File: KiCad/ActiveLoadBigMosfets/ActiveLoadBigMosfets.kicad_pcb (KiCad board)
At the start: 2 copper layers, 145 x 70 mm, 170 parts, among them J1 TouchPanel, J2 PowerInput, J3 SWD, J4 RVT28AETNWC00, J5 JTAG, J6 FanOut, J7 PowerInput2, J8 PowerInput3, J9 PowerInput4, Q1 IRLML2502, Q10 IXFK44N50P, Q11 IXFK44N50P, Q12 IXFK44N50P, Q13 IXFK44N50P, Q14 IXFK44N50P, Q2 IRLML2244, Q3 IRLML2244, Q4 IRLML2502, Q5 IRLML2502, Q6 IRLML2502, Q7 IRLML2502, Q8 IRLML2502, Q9 IXFK44N50P, SW1 Rotary_Encoder_Switch, SW2 SW_Push, U1 LMR14020, U2 MCP1825S, U3 STM32L151RBTxA, U4 LM2735YMF, U5 TLV2374, U6 TLV2374, U7 TLV2374, U8 TC74, U9 INA233, Y1 Crystal

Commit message: More pcb work
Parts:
- added J10: I2C, Connector_PinHeader_2.54mm:PinHeader_1x04_P2.54mm_Vertical, F.Cu at (82.5, 31.0)
- C38, U9: moved to F.Cu
- FL1, FL2: footprint Filter:Filter_Murata_BNX025 -> JPInductors:Filter_Murata_BNX025
- L3: footprint Inductor_SMD:L_Wuerth_WE-PDF -> JPInductors:L_Wuerth_WE-PDF_Handsoldering
- R1, R43, R45, R46, R49, R50, R55, R63: footprint Resistor_SMD:R_2512_6332Metric -> Resistor_SMD:R_2512_6332Metric_Pad1.52x3.35mm_HandSolder
- U4: footprint Package_TO_SOT_SMD:SOT-23-5 -> Package_TO_SOT_SMD:SOT-23-5_HandSoldering
- moved C19 24.3 mm to (60.6, 60.8)
- moved C20 24.3 mm to (58.7, 60.8)
- moved C22 24.3 mm to (72.0, 60.8)
- moved FL1 24.3 mm to (47.0, 61.6)
- moved U2 24.3 mm to (65.7, 60.8)
- moved C21 24.3 mm to (75.6, 61.0)
- moved L2 20.3 mm to (24.8, 54.0), turned to 0 degrees
- moved R9 19.9 mm to (38.5, 44.6), turned to 90 degrees
- moved R11 18.9 mm to (37.3, 34.7), turned to 0 degrees
- moved R13 18.2 mm to (37.8, 37.8), turned to 270 degrees
- moved R14 18.1 mm to (37.8, 41.4), turned to 90 degrees
- moved C10 17.2 mm to (36.4, 44.6), turned to 90 degrees
- moved C13 17.1 mm to (31.1, 29.8), turned to 180 degrees
- moved C9 15.0 mm to (34.2, 34.9), turned to 180 degrees
- moved C16 14.0 mm to (34.0, 44.5), turned to 180 degrees
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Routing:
- net +4V: track 107.3 -> 47.3 mm
- net GNDD: track 593.5 -> 546.2 mm, vias 23 -> 22
- net Net-(C10-Pad1): track 55.2 -> 11.4 mm
- net GND: track 225.7 -> 188.3 mm
- net PowerIn+: track 11.9 -> 21.5 mm, vias 0 -> 1
- net +3V3: track 280.6 -> 287.5 mm, vias 20 -> 22
- net PowerIn-: track 239.0 -> 232.7 mm, vias 0 -> 1
- net SCL: track 98.0 -> 102.0 mm, vias 6 -> 5
- net Net-(C8-Pad1): track 17.2 -> 13.7 mm
- net SDA: track 100.3 -> 102.7 mm, vias 4 -> 3
- net Net-(C8-Pad2): track 2.31 -> 0.00 mm
- net GNDA: track 192.1 -> 190.1 mm
- net TP_Interrupt: track 25.9 -> 24.3 mm
- net TP_Reset: track 26.9 -> 25.6 mm
- net SWCLK: track 85.3 -> 84.3 mm
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- removed copper zone on B.Cu, net GND
- removed copper zone on F.Cu, net GND

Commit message: More pcb work
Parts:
- J10: moved to B.Cu
- R48, R53, R54, R56, R57, R61: moved to F.Cu
- moved C37 38.5 mm to (84.1, 18.8)
- moved U8 38.5 mm to (89.8, 21.3)
- moved R60 3.70 mm to (106.5, 19.3)
- moved D4 3.70 mm to (106.4, 21.7)
- moved C33 3.36 mm to (70.1, 15.5)
- moved C34 3.19 mm to (71.9, 15.5)
- moved R38 2.82 mm to (23.9, 9.14)
- moved R39 2.82 mm to (26.9, 9.14)
- moved R40 2.82 mm to (69.6, 9.14)
- moved R41 2.82 mm to (72.6, 9.14)
- moved R44 2.82 mm to (119.6, 9.14)
- moved R42 2.82 mm to (116.6, 9.14)
- moved C36 2.59 mm to (118.9, 15.5)
- moved C35 2.55 mm to (117.1, 15.5)
- moved R26 2.54 mm to (20.3, 14.0)
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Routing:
- net PowerIn-: track 232.7 -> 164.7 mm
- net LoadLevel: track 138.2 -> 120.4 mm, vias 9 -> 6
- net GNDA: track 190.1 -> 172.7 mm, vias 7 -> 4
- net GNDD: track 546.2 -> 529.7 mm, vias 22 -> 21
- net +3V3: track 287.5 -> 276.5 mm, vias 22 -> 21
- net LED: track 42.2 -> 31.2 mm
- net SDA: track 102.7 -> 92.6 mm
- net SCL: track 102.0 -> 93.2 mm
- net +12V: track 182.2 -> 176.1 mm
- net GND: track 188.3 -> 193.4 mm
- net Net-(Q10-Pad3): track 9.67 -> 14.0 mm, vias 0 -> 1
- net Net-(Q12-Pad3): track 10.7 -> 14.6 mm, vias 0 -> 1
- net Net-(C39-Pad2): track 8.35 -> 11.5 mm, vias 0 -> 1
- net Net-(Q14-Pad3): track 10.7 -> 13.7 mm, vias 0 -> 1
- net Net-(Q11-Pad3): track 20.8 -> 23.4 mm
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
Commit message: PCB work
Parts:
- added REF**: RVT28AETNWC00-Folded, JPDisplays:RVT28AETNWC00-Folded, F.Cu at (72.9, 69.8)
- J4: footprint JPConnectors:Hirose_FH12-50S-0.5SH_1x50-1MP_P0.50mm_Horizontal -> JPConnectors:Molex-50S-0.5SH_1x50-P0.50mm_Horizontal
- SW2: footprint Button_Switch_SMD:SW_SPST_EVQP0 -> Button_Switch_SMD:SW_SPST_B3S-1000
- U8: footprint Package_TO_SOT_THT:TO-220-5_Vertical -> Connector_PinHeader_2.54mm:PinHeader_1x05_P2.54mm_Vertical
- moved J10 48.7 mm to (34.5, 22.6)
- moved C37 44.4 mm to (39.6, 18.8), turned to 270 degrees
- moved U8 37.7 mm to (52.3, 17.5), turned to 90 degrees
- moved C29 20.7 mm to (121.4, 59.1), turned to 270 degrees
- moved C24 16.2 mm to (72.4, 48.0), turned to 270 degrees
- moved C15 14.9 mm to (75.7, 31.9), turned to 90 degrees
- moved R65 14.5 mm to (77.1, 31.9), turned to 90 degrees
- moved R64 14.3 mm to (78.5, 31.9), turned to 90 degrees
- moved C27 13.8 mm to (116.7, 61.0), turned to 270 degrees
- moved R19 12.8 mm to (70.9, 48.0), turned to 270 degrees
- moved C14 11.5 mm to (115.1, 61.0), turned to 270 degrees
- moved D2 11.3 mm to (113.8, 57.1), turned to 180 degrees
- moved L3 11.1 mm to (104.9, 54.0), turned to 0 degrees
- moved R25 10.9 mm to (114.3, 63.5), turned to 180 degrees
- moved C26 10.4 mm to (112.5, 66.0), turned to 90 degrees
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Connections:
- U3 pad 49: Net-(U3-Pad49) -> /LCD_RESET
- U3 pad 50: /LCD_RESET -> Net-(U3-Pad50)
- U8 pad 2: SCL -> SDA
- U8 pad 4: SDA -> SCL
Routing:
- net +4V: track 47.3 -> 104.4 mm, vias 4 -> 6
- net TP_X_Ctrl: track 3.03 -> 54.7 mm, vias 0 -> 2
- net TP_Y_Ctrl: track 3.42 -> 51.4 mm, vias 0 -> 2
- net TP_SenseX-: track 8.03 -> 55.2 mm, vias 1 -> 2
- net GNDD: track 529.7 -> 574.4 mm, vias 21 -> 25
- net TP_SenseY-: track 12.7 -> 55.9 mm, vias 1 -> 2
- net GND: track 193.4 -> 229.8 mm, vias 1 -> 2
- net Net-(C10-Pad1): track 11.4 -> 44.5 mm
- net InaAlert: track 70.9 -> 50.2 mm, vias 7 -> 3
- net PowerIn-: track 164.7 -> 184.0 mm
- net Net-(R64-Pad2): track 36.9 -> 53.4 mm
- net +12V: track 176.1 -> 160.9 mm, vias 5 -> 7
- net LED: track 31.2 -> 43.7 mm
- net FanPWD: track 35.7 -> 48.1 mm
- net FanSensor: track 35.3 -> 46.8 mm
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- added copper zone on B.Cu, net GND
- added copper zone on F.Cu, net GND
- added copper zone on B.Cu, net GNDD
- added copper zone on F.Cu, net GNDD
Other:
- board size 145 x 70 mm -> 144.8 x 70 mm
- net class DigitalPower added: clearance 0.14, trace_width 0.6096, via_dia 0.6, via_drill 0.4
- board text added: "1"
- board text added: "3V3"
- board text added: "50"
- board text added: "6"
- board text added: "ActveLoadBigMosfet v1 JP, 10.04.2020"
- board text added: "Fan"
- board text added: "Gnd"
- board text added: "JTAG"
- board text added: "NRST"
- board text added: "SCL"
- board text added: "SDA"
- board text added: "STM32L151RBTxA"
- board text added: "SWCLK"
- board text added: "SWD"
- board text added: "SWDIO"
- board text added: "SWDO"
- board text added: "nc"

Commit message: PCB work
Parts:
- removed REF**: RVT28AETNWC00-Folded, JPDisplays:RVT28AETNWC00-Folded
- moved R43 1.40 mm to (13.3, 9.65)
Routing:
- net Net-(Q9-Pad3): track 24.0 -> 27.9 mm
- net GND: track 229.8 -> 229.3 mm
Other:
- board text added: "ActiveLoadBigMosfets v1 JP, 10.04.2020"
- board text removed: "ActveLoadBigMosfet v1 JP, 10.04.2020"

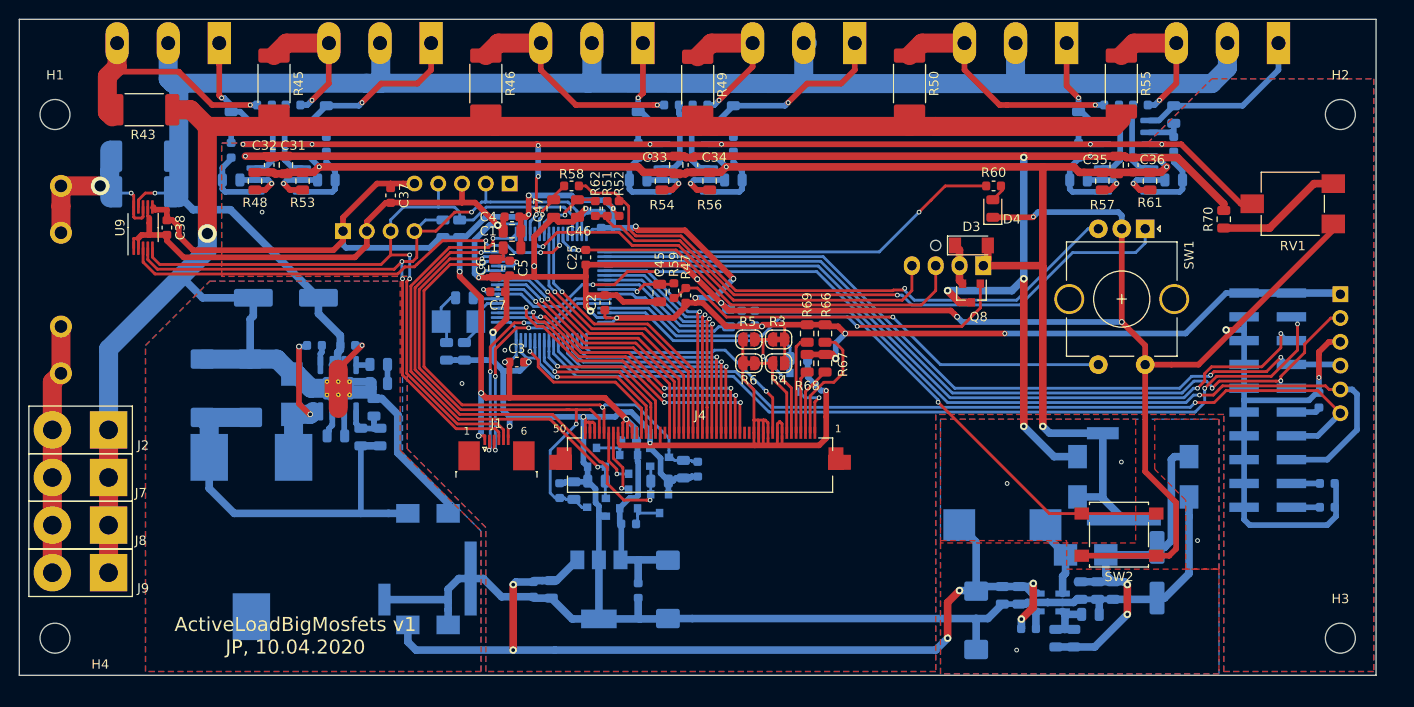
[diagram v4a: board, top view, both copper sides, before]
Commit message: Latest PCB changes. STM32 Project
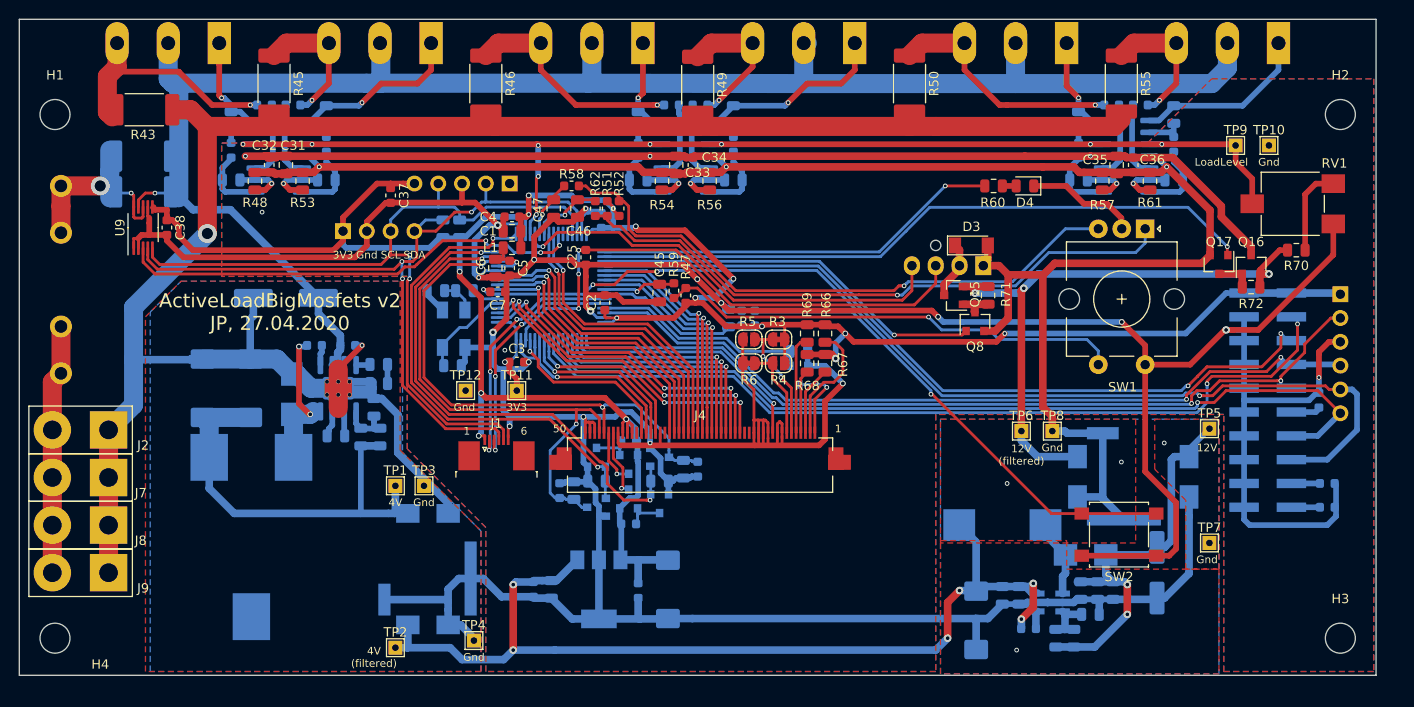
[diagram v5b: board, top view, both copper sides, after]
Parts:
- added Q15: IRLML2244, Package_TO_SOT_SMD:SOT-23, F.Cu at (99.7, 29.5)
- added Q16: IRLML2244, Package_TO_SOT_SMD:SOT-23, F.Cu at (131.4, 26.2)
- added Q17: IRLML2502, Package_TO_SOT_SMD:SOT-23, F.Cu at (128.0, 26.2)
- added R71: 100k, Resistor_SMD:R_0805_2012Metric, F.Cu at (103.4, 29.5)
- added R72: 100k, Resistor_SMD:R_0805_2012Metric, F.Cu at (131.4, 28.6)
- added TP1: TestPoint, TestPoint:TestPoint_THTPad_1.5x1.5mm_Drill0.7mm, F.Cu at (40.1, 49.8)
- added TP10: TestPoint, TestPoint:TestPoint_THTPad_1.5x1.5mm_Drill0.7mm, F.Cu at (133.3, 13.5)
- added TP11: TestPoint, TestPoint:TestPoint_THTPad_1.5x1.5mm_Drill0.7mm, F.Cu at (53.1, 39.6)
- added TP12: TestPoint, TestPoint:TestPoint_THTPad_1.5x1.5mm_Drill0.7mm, F.Cu at (47.6, 39.6)
- added TP2: TestPoint, TestPoint:TestPoint_THTPad_1.5x1.5mm_Drill0.7mm, F.Cu at (40.1, 67.1)
- added TP3: TestPoint, TestPoint:TestPoint_THTPad_1.5x1.5mm_Drill0.7mm, F.Cu at (43.2, 49.8)
- added TP4: TestPoint, TestPoint:TestPoint_THTPad_1.5x1.5mm_Drill0.7mm, F.Cu at (48.5, 66.3)
- added TP5: TestPoint, TestPoint:TestPoint_THTPad_1.5x1.5mm_Drill0.7mm, F.Cu at (127.0, 43.7)
- added TP6: TestPoint, TestPoint:TestPoint_THTPad_1.5x1.5mm_Drill0.7mm, F.Cu at (106.9, 43.9)
- added TP7: TestPoint, TestPoint:TestPoint_THTPad_1.5x1.5mm_Drill0.7mm, F.Cu at (127.0, 55.9)
- added TP8: TestPoint, TestPoint:TestPoint_THTPad_1.5x1.5mm_Drill0.7mm, F.Cu at (110.2, 43.9)
- added TP9: TestPoint, TestPoint:TestPoint_THTPad_1.5x1.5mm_Drill0.7mm, F.Cu at (129.8, 13.5)
- R60: value 10k -> 4k7; footprint Resistor_SMD:R_0603_1608Metric -> Resistor_SMD:R_0805_2012Metric
- R7, R8: value 2k2 -> 4k7
- Y1: value Crystal -> 16MHz; footprint Crystal:Crystal_SMD_5032-2Pin_5.0x3.2mm -> Crystal:Crystal_SMD_Abracon_ABM3B-4Pin_5.0x3.2mm
- moved R70 8.42 mm to (136.3, 24.6), turned to 0 degrees
- moved C18 6.58 mm to (44.5, 29.0), turned to 180 degrees
- moved D4 4.19 mm to (107.3, 17.8), turned to 180 degrees
- moved Q8 3.07 mm to (102.0, 32.3), turned to 90 degrees
- moved C17 1.98 mm to (46.2, 37.0), turned to 0 degrees
- moved Y1 0.92 mm to (46.4, 33.0), turned to 90 degrees
- moved Q1 0.76 mm to (83.2, 38.0)
- moved R15 0.76 mm to (47.5, 29.0)
- moved R2 0.76 mm to (83.2, 35.4)
- turned C33 to 90 degrees
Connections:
- net FanPWD renamed FanPWM
- C31 pad 1: +12V -> LoadOpAmpsPower
- C32 pad 1: +12V -> LoadOpAmpsPower
- C33 pad 1: +12V -> GNDA
- C33 pad 2: GNDA -> LoadOpAmpsPower
- C34 pad 1: +12V -> LoadOpAmpsPower
- C35 pad 1: +12V -> LoadOpAmpsPower
- C36 pad 1: +12V -> LoadOpAmpsPower
- Q8 pad 1: FanPower -> FanPowerCtrl
- Q8 pad 2: Net-(D3-Pad1) -> GNDA
- Q8 pad 3: +12V -> Net-(Q15-Pad1)
- U3 pad 27: FanSensor -> Net-(U3-Pad27)
- U3 pad 34: SWDIO -> LoadOpAmpsPowerCtrl
- U3 pad 35: SWCLK -> FanPowerCtrl
- U3 pad 45: FanPower -> DisplayLEDCtrl
- U3 pad 46: DisplayLEDCtrl -> SWDIO
- U3 pad 49: /LCD_RESET -> SWCLK
- U3 pad 50: Net-(U3-Pad50) -> /LCD_RESET
- U3 pad 62: Net-(U3-Pad62) -> FanSensor
- U5 pad 4: +12V -> LoadOpAmpsPower
- U6 pad 4: +12V -> LoadOpAmpsPower
- U7 pad 4: +12V -> LoadOpAmpsPower
- Y1 pad 2: Net-(C18-Pad1) -> GNDD
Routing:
- net LoadOpAmpsPower: track 0.00 -> 118.9 mm, vias 0 -> 3
- net +12V: track 160.9 -> 65.3 mm, vias 7 -> 3
- net LoadOpAmpsPowerCtrl: track 0.00 -> 71.3 mm, vias 0 -> 1
- net FanPower: track 46.0 -> 0.00 mm, vias 1 -> 0
- net FanPowerCtrl: track 0.00 -> 42.0 mm, vias 0 -> 1
- net GNDA: track 162.8 -> 189.2 mm, vias 4 -> 3
- net FanSensor: track 46.8 -> 57.5 mm, vias 1 -> 3
- net Net-(R70-Pad2): track 13.7 -> 9.44 mm
- net GNDD: track 574.7 -> 570.5 mm, vias 25 -> 23
- net Net-(Q16-Pad1): track 0.00 -> 3.90 mm
- net Net-(C17-Pad1): track 6.34 -> 10.1 mm
- net Net-(Q15-Pad1): track 0.00 -> 3.56 mm
- net Net-(C14-Pad1): track 39.2 -> 42.7 mm
- net Net-(C10-Pad1): track 44.5 -> 47.5 mm
- net LoadLevel: track 128.0 -> 130.7 mm
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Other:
- board text added: "12V"
- board text added: "12V (filtered)"
- board text added: "4V"
- board text added: "4V (filtered)"
- board text added: "ActiveLoadBigMosfets v2 JP, 27.04.2020"
- board text added: "LoadLevel"
- board text removed: "ActiveLoadBigMosfets v1 JP, 10.04.2020"

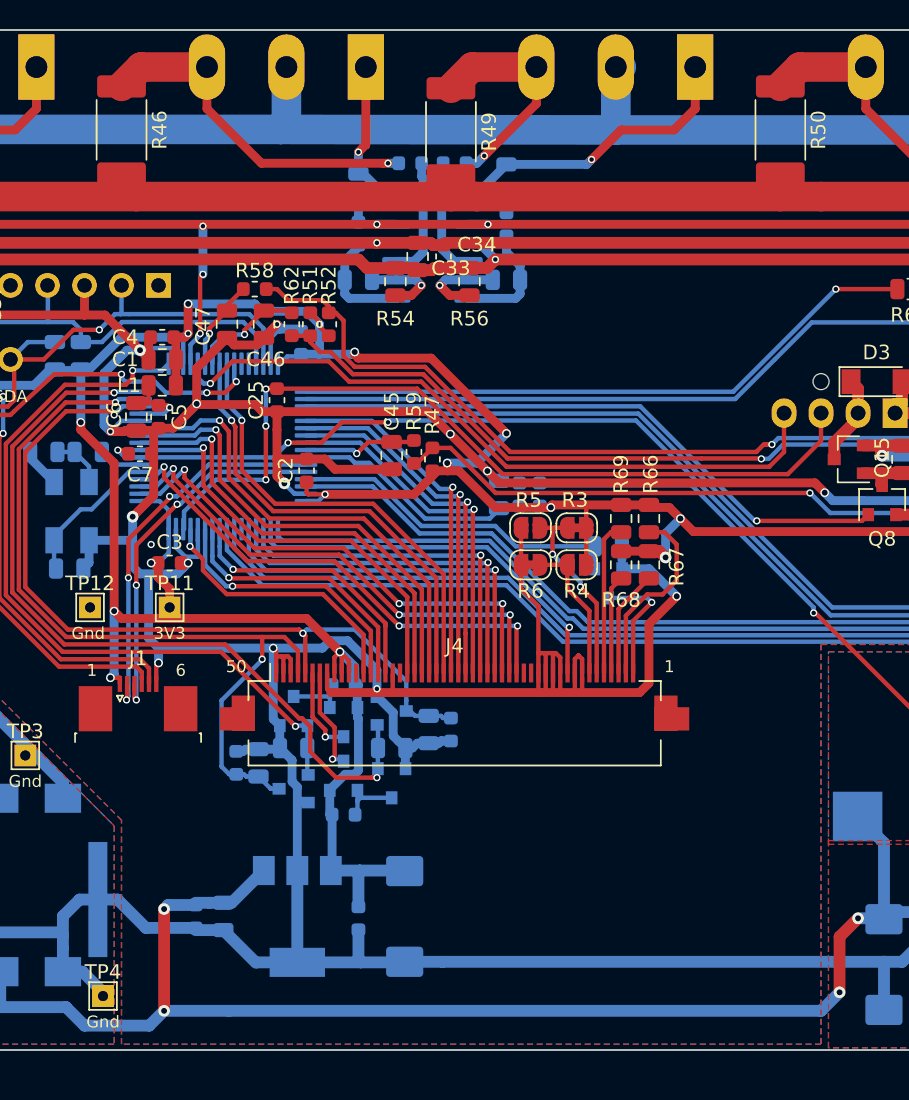
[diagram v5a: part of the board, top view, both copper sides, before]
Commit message: Debug screen added
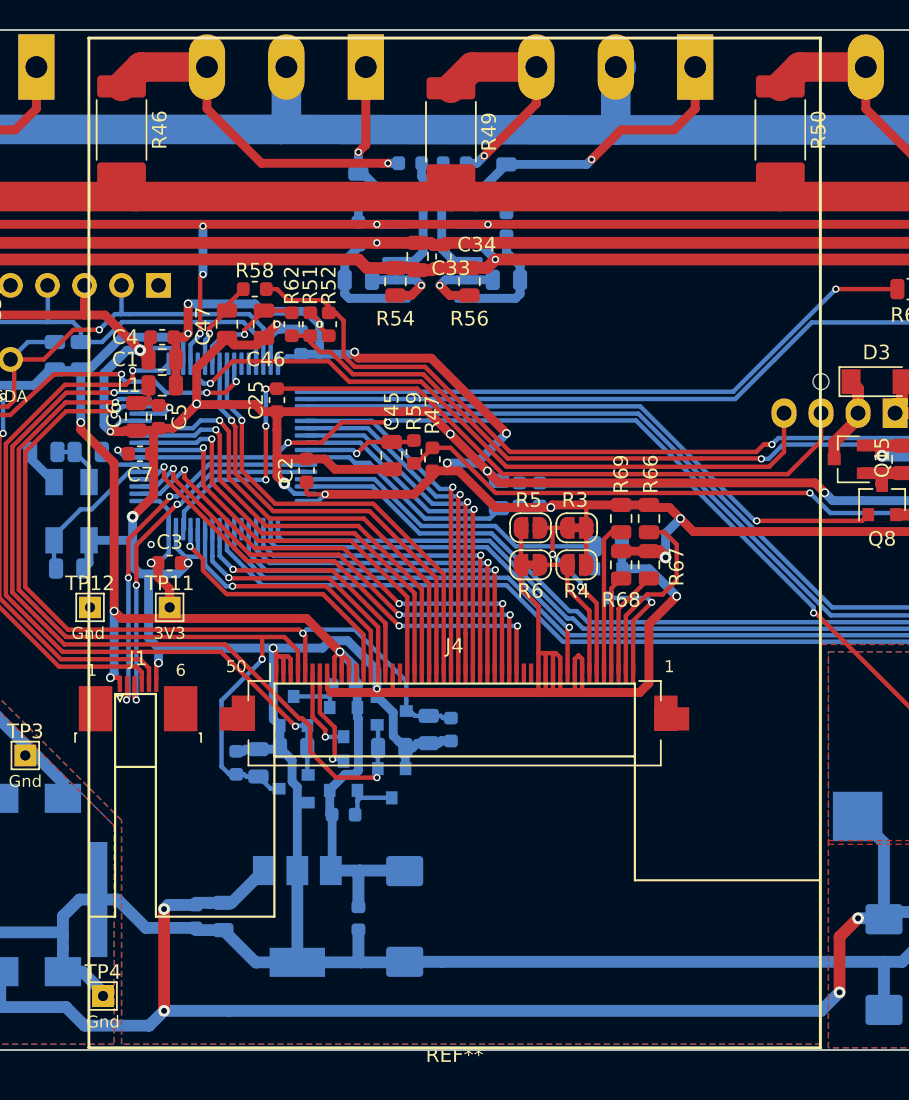
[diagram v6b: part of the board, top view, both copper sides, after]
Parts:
- added REF**: RVT28AETNWC00-Folded, JPDisplays:RVT28AETNWC00-Folded, F.Cu at (72.6, 69.8)
